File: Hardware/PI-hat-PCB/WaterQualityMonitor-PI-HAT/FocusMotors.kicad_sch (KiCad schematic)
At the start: 1 part

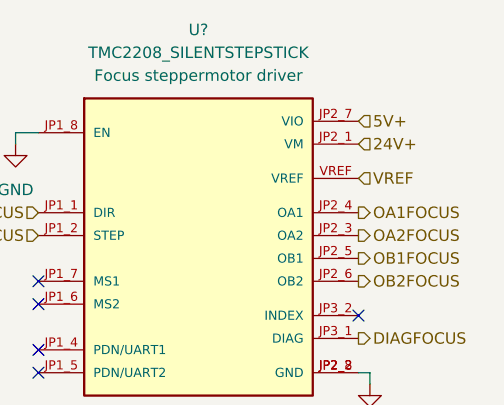
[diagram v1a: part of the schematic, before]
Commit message: Enhanced schematics
Moved protection circuits to main schematic
changed tmc2208 VIO to 3.3V (5V is also fine)
added fuses to heat and cooling schematic
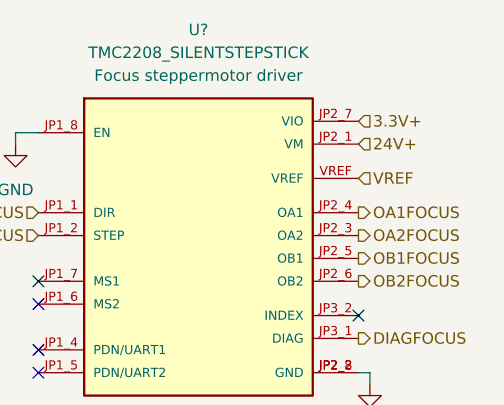
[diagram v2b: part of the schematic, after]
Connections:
- net 5V+ renamed 3.3V+
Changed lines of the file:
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@@
-    (effects (font (size 1.27 1.27)) (justify left))
-  )
-  (hierarchical_label "5V+" (shape input) (at 163.83 92.71 0)
     (effects (font (size 1.27 1.27)) (justify left))
   )
@@
     (effects (font (size 1.27 1.27)) (justify left))
   )
+  (hierarchical_label "3.3V+" (shape input) (at 163.83 92.71 0)
+    (effects (font (size 1.27 1.27)) (justify left))
+  )

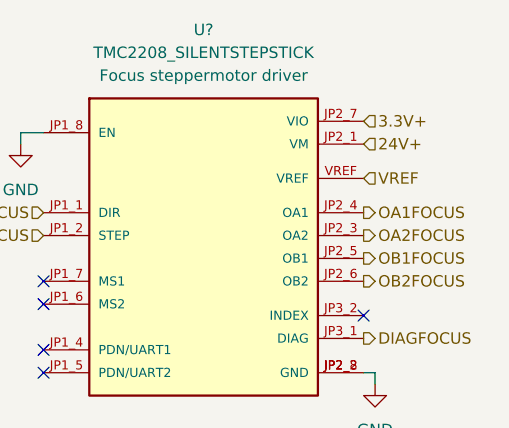
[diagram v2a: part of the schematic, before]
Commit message: changed PSU voltage from 24V to 12V
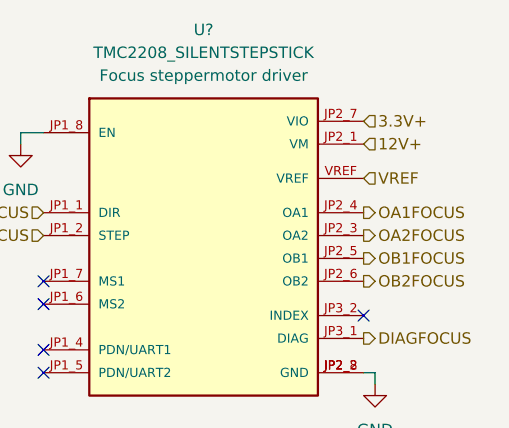
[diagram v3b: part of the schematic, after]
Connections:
- net 24V+ renamed 12V+
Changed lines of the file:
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@@
     (effects (font (size 1.27 1.27)) (justify right))
   )
-  (hierarchical_label "24V+" (shape input) (at 163.83 95.25 0)
+  (hierarchical_label "12V+" (shape input) (at 163.83 95.25 0)
     (effects (font (size 1.27 1.27)) (justify left))
   )

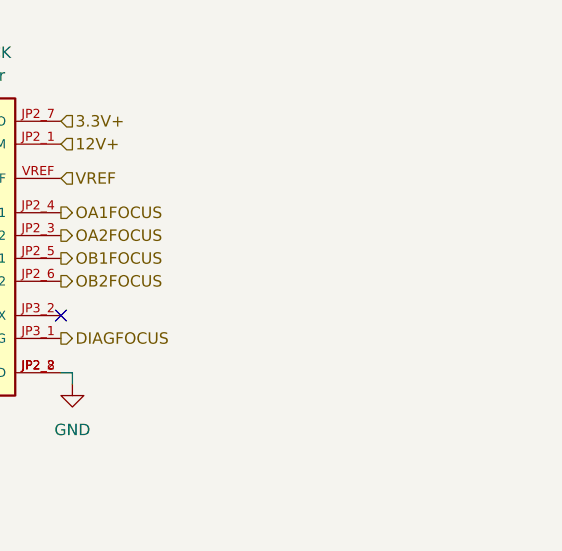
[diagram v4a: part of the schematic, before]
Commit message: added drv8838 in design as option for focussing motors
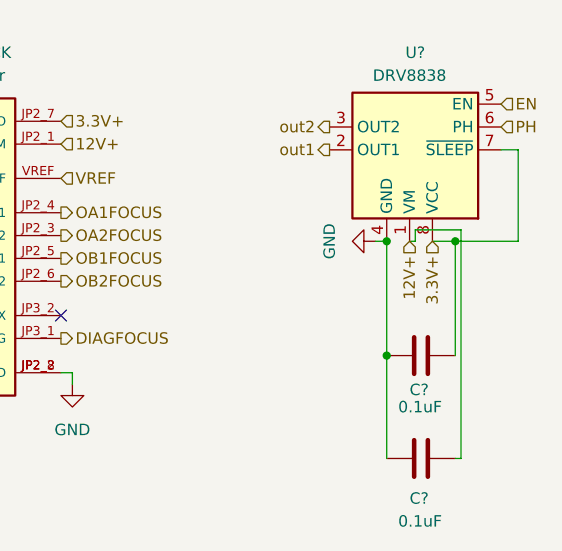
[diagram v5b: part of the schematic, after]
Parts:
- added C? (x2): 0.1uF, symbol Device:C
- added U?: DRV8838, Package_SON:WSON-8-1EP_2x2mm_P0.5mm_EP0.9x1.6mm, symbol Driver_Motor:DRV8838
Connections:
- net 12V+: now also C?.2, U?.1 (VM)
- net 3.3V+: now also C?.2, U?.7 (~{SLEEP}), U?.8 (VCC)
- net GND: now also C?.1, C?.1, U?.4 (GND), U?.9 (GND)
- new net EN: U?.5 (EN)
- new net PH: U?.6 (PH)
- new net out1: U?.2 (OUT1)
- new net out2: U?.3 (OUT2)
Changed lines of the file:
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@@
 (kicad_sch (version 20211123) (generator eeschema)
   (paper "A4")
+  (junction (at 207.645 106.045) (diameter 0) (color 0 0 0 0)
+  )
+  (junction (at 200.025 118.745) (diameter 0) (color 0 0 0 0)
+  )
+  (junction (at 200.025 106.045) (diameter 0) (color 0 0 0 0)
+  )
   (no_connect (at 163.83 114.3))
   (no_connect (at 128.27 118.11))
@@
   (no_connect (at 128.27 110.49))
   (no_connect (at 128.27 113.03))
+  (wire (pts (xy 214.63 106.045) (xy 214.63 95.885))
+    (stroke (width 0) (type default) (color 0 0 0 0))
+  )
+  (wire (pts (xy 214.63 95.885) (xy 212.725 95.885))
+    (stroke (width 0) (type default) (color 0 0 0 0))
+  )
+  (wire (pts (xy 205.105 106.045) (xy 207.645 106.045))
+    (stroke (width 0) (type default) (color 0 0 0 0))
+  )
+  (wire (pts (xy 207.645 106.045) (xy 207.645 118.745))
+    (stroke (width 0) (type default) (color 0 0 0 0))
+  )
+  (wire (pts (xy 208.28 130.175) (xy 207.645 130.175))
+    (stroke (width 0) (type default) (color 0 0 0 0))
+  )
+  (wire (pts (xy 198.755 106.045) (xy 200.025 106.045))
+    (stroke (width 0) (type default) (color 0 0 0 0))
+  )
   (wire (pts (xy 165.1 121.92) (xy 165.1 120.65))
     (stroke (width 0) (type default) (color 0 0 0 0))
@@
     (stroke (width 0) (type default) (color 0 0 0 0))
   )
+  (wire (pts (xy 203.2 106.045) (xy 203.2 104.775))
+    (stroke (width 0) (type default) (color 0 0 0 0))
+  )
   (wire (pts (xy 125.73 93.98) (xy 125.73 95.25))
     (stroke (width 0) (type default) (color 0 0 0 0))
   )
+  (wire (pts (xy 200.025 106.045) (xy 200.025 118.745))
+    (stroke (width 0) (type default) (color 0 0 0 0))
+  )
+  (wire (pts (xy 208.28 104.775) (xy 208.28 130.175))
+    (stroke (width 0) (type default) (color 0 0 0 0))
+  )
+  (wire (pts (xy 202.565 106.045) (xy 203.2 106.045))
+    (stroke (width 0) (type default) (color 0 0 0 0))
+  )
+  (wire (pts (xy 207.645 106.045) (xy 214.63 106.045))
+    (stroke (width 0) (type default) (color 0 0 0 0))
+  )
+  (wire (pts (xy 203.2 104.775) (xy 208.28 104.775))
+    (stroke (width 0) (type default) (color 0 0 0 0))
+  )
   (wire (pts (xy 165.1 120.65) (xy 163.83 120.65))
     (stroke (width 0) (type default) (color 0 0 0 0))
   )
+  (wire (pts (xy 200.025 118.745) (xy 200.025 130.175))
+    (stroke (width 0) (type default) (color 0 0 0 0))
+  )
   (hierarchical_label "VREF" (shape input) (at 163.83 99.06 0)
     (effects (font (size 1.27 1.27)) (justify left))
@@
     (effects (font (size 1.27 1.27)) (justify left))
   )
+  (hierarchical_label "out2" (shape output) (at 193.675 93.345 180)
+    (effects (font (size 1.27 1.27)) (justify right))
+  )
+  (hierarchical_label "12V+" (shape input) (at 202.565 106.045 270)
+    (effects (font (size 1.27 1.27)) (justify right))
+  )
   (hierarchical_label "3.3V+" (shape input) (at 163.83 92.71 0)
     (effects (font (size 1.27 1.27)) (justify left))
@@
     (effects (font (size 1.27 1.27)) (justify left))
   )
+  (hierarchical_label "out1" (shape output) (at 193.675 95.885 180)
+    (effects (font (size 1.27 1.27)) (justify right))
+  )
   (hierarchical_label "STEPFOCUS" (shape input) (at 128.27 105.41 180)
     (effects (font (size 1.27 1.27)) (justify right))
@@
   (hierarchical_label "12V+" (shape input) (at 163.83 95.25 0)
     (effects (font (size 1.27 1.27)) (justify left))
+  )
+  (hierarchical_label "EN" (shape input) (at 212.725 90.805 0)
+    (effects (font (size 1.27 1.27)) (justify left))
+  )
+  (hierarchical_label "PH" (shape input) (at 212.725 93.345 0)
+    (effects (font (size 1.27 1.27)) (justify left))
+  )
+  (hierarchical_label "3.3V+" (shape input) (at 205.105 106.045 270)
+    (effects (font (size 1.27 1.27)) (justify right))
   )
   (symbol (lib_name "TMC2208_SILENTSTEPSTICK_1") (lib_id "TMC2208_SILENTSTEPSTICK:TMC2208_SILENTSTEPSTICK") (at 146.05 107.95 0) (unit 1)
@@
     (pin "VREF")
   )
+  (symbol (lib_id "Device:C") (at 203.835 130.175 90) (unit 1)
+    (in_bom yes) (on_board yes)
+    (property "Reference" "C?" (id 0) (at 202.565 134.62 90)
+      (effects (font (size 1.27 1.27)) (justify right))
+    )
+    (property "Value" "0.1uF" (id 1) (at 201.295 137.16 90)
+      (effects (font (size 1.27 1.27)) (justify right))
+    )
+    (property "Footprint" "" (id 2) (at 207.645 129.2098 0)
+      (effects (font (size 1.27 1.27)) hide)
+    )
+    (property "Datasheet" "~" (id 3) (at 203.835 130.175 0)
+      (effects (font (size 1.27 1.27)) hide)
+    )
+    (pin "1")
+    (pin "2")
+  )
   (symbol (lib_id "power:GND") (at 125.73 95.25 0) (unit 1)
     (in_bom yes) (on_board yes) (fields_autoplaced)
@@
     (pin "1")
   )
+  (symbol (lib_id "power:GND") (at 198.755 106.045 270) (unit 1)
+    (in_bom yes) (on_board yes) (fields_autoplaced)
+    (property "Reference" "#PWR?" (id 0) (at 192.405 106.045 0)
+      (effects (font (size 1.27 1.27)) hide)
+    )
+    (property "Value" "GND" (id 1) (at 193.675 106.045 0))
+    (property "Footprint" "" (id 2) (at 198.755 106.045 0)
+      (effects (font (size 1.27 1.27)) hide)
+    )
+    (property "Datasheet" "" (id 3) (at 198.755 106.045 0)
+      (effects (font (size 1.27 1.27)) hide)
+    )
+    (pin "1")
+  )
+  (symbol (lib_id "Driver_Motor:DRV8838") (at 202.565 93.345 180) (unit 1)
+    (in_bom yes) (on_board yes)
+    (property "Reference" "U?" (id 0) (at 203.2 85.09 0))
+    (property "Value" "DRV8838" (id 1) (at 202.565 87.63 0))
+    (property "Footprint" "Package_SON:WSON-8-1EP_2x2mm_P0.5mm_EP0.9x1.6mm" (id 2) (at 224.155 93.345 0)
+      (effects (font (size 1.27 1.27)) hide)
+    )
+    (property "Datasheet" "http://www.ti.com/lit/ds/symlink/drv8837.pdf" (id 3) (at 202.565 93.345 0)
+      (effects (font (size 1.27 1.27)) hide)
+    )
+    (pin "1")
+    (pin "2")
+    (pin "3")
+    (pin "4")
+    (pin "5")
+    (pin "6")
+    (pin "7")
+    (pin "8")
+    (pin "9")
+  )
+  (symbol (lib_id "Device:C") (at 203.835 118.745 90) (unit 1)
+    (in_bom yes) (on_board yes)
+    (property "Reference" "C?" (id 0) (at 202.565 122.555 90)
+      (effects (font (size 1.27 1.27)) (justify right))
+    )
+    (property "Value" "0.1uF" (id 1) (at 201.295 124.46 90)
+      (effects (font (size 1.27 1.27)) (justify right))
+    )
+    (property "Footprint" "" (id 2) (at 207.645 117.7798 0)
+      (effects (font (size 1.27 1.27)) hide)
+    )
+    (property "Datasheet" "~" (id 3) (at 203.835 118.745 0)
+      (effects (font (size 1.27 1.27)) hide)
+    )
+    (pin "1")
+    (pin "2")
+  )
   (symbol (lib_id "power:GND") (at 165.1 121.92 0) (unit 1)

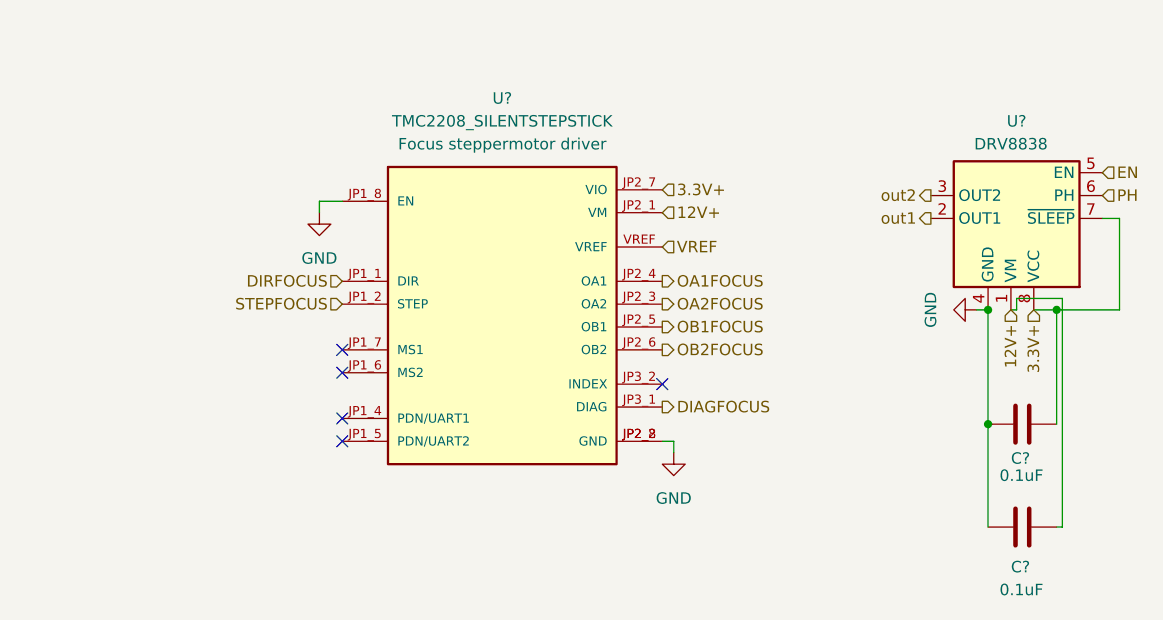
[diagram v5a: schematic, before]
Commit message: added terminal drv8838 design
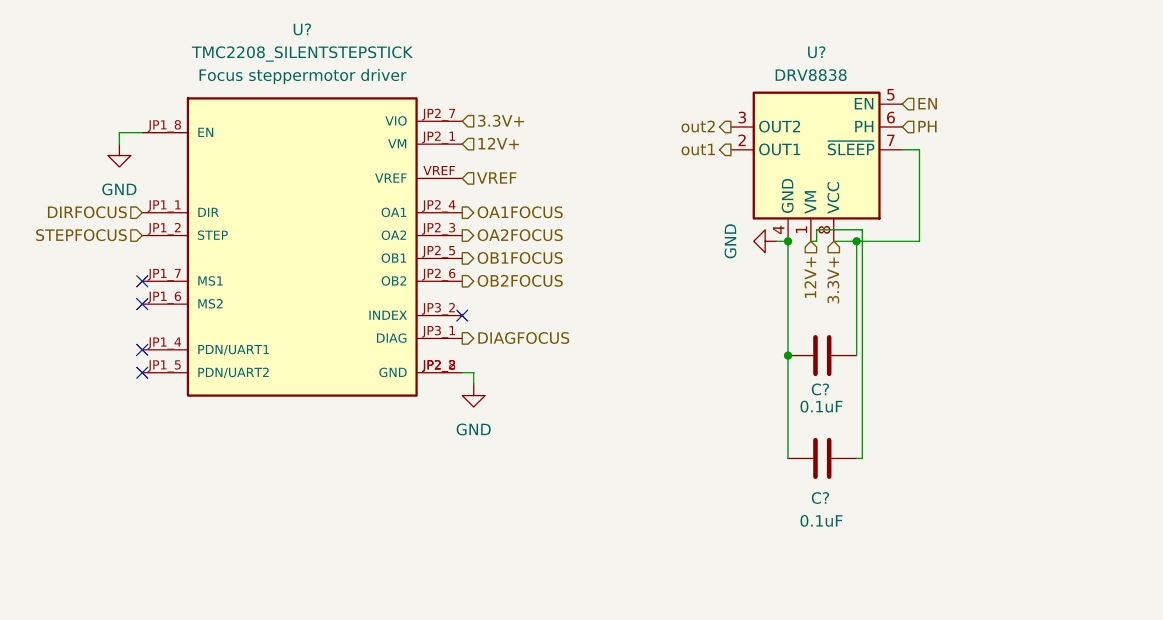
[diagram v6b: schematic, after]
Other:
- moved on the sheet: C?, U?

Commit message: RPI integration
Connected RPI to all motors, sensors etc.
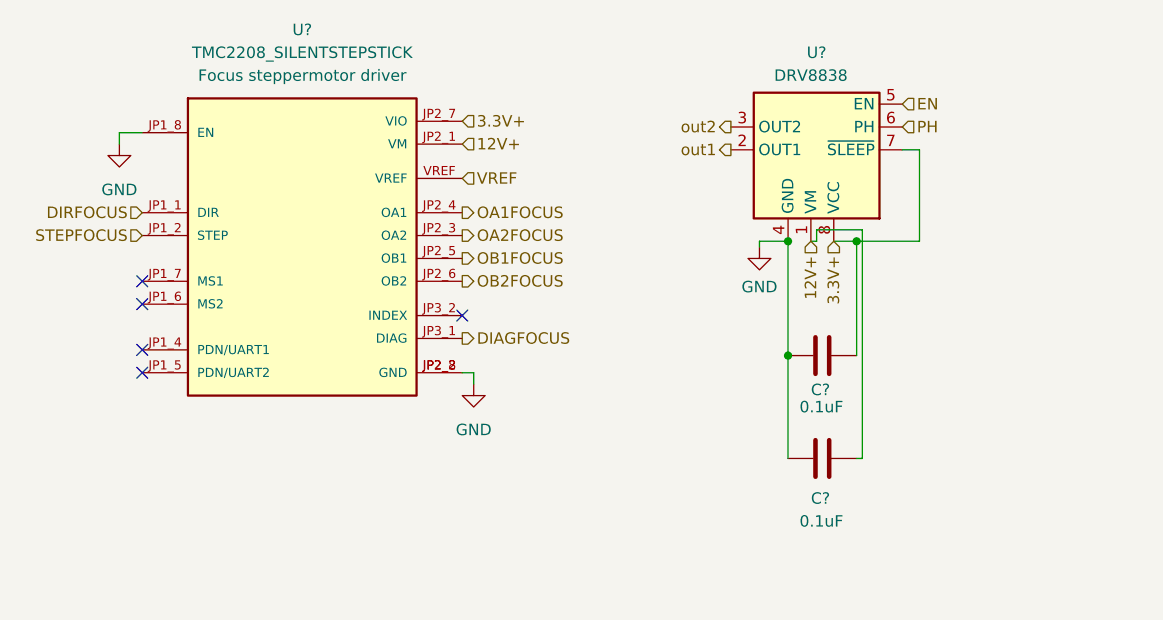
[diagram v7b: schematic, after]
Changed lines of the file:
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@@
     (stroke (width 0) (type default) (color 0 0 0 0))
   )
-  (wire (pts (xy 176.53 98.425) (xy 177.8 98.425))
+  (wire (pts (xy 174.625 98.425) (xy 177.8 98.425))
     (stroke (width 0) (type default) (color 0 0 0 0))
   )
@@
   )
   (wire (pts (xy 106.045 86.36) (xy 103.505 86.36))
+    (stroke (width 0) (type default) (color 0 0 0 0))
+  )
+  (wire (pts (xy 174.625 98.425) (xy 174.625 99.06))
     (stroke (width 0) (type default) (color 0 0 0 0))
   )
@@
     (pin "1")
   )
-  (symbol (lib_id "power:GND") (at 176.53 98.425 270) (unit 1)
+  (symbol (lib_id "power:GND") (at 174.625 99.06 0) (unit 1)
     (in_bom yes) (on_board yes) (fields_autoplaced)
-    (property "Reference" "#PWR?" (id 0) (at 170.18 98.425 0)
+    (property "Reference" "#PWR?" (id 0) (at 174.625 105.41 0)
       (effects (font (size 1.27 1.27)) hide)
     )
-    (property "Value" "GND" (id 1) (at 171.45 98.425 0))
-    (property "Footprint" "" (id 2) (at 176.53 98.425 0)
+    (property "Value" "GND" (id 1) (at 174.625 103.505 0))
+    (property "Footprint" "" (id 2) (at 174.625 99.06 0)
       (effects (font (size 1.27 1.27)) hide)
     )
-    (property "Datasheet" "" (id 3) (at 176.53 98.425 0)
+    (property "Datasheet" "" (id 3) (at 174.625 99.06 0)
       (effects (font (size 1.27 1.27)) hide)
     )
